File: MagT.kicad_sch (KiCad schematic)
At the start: 6 parts, among them IC6 DRV8212DSGR, IC7 DRV8212DSGR, IC8 DRV8212DSGR

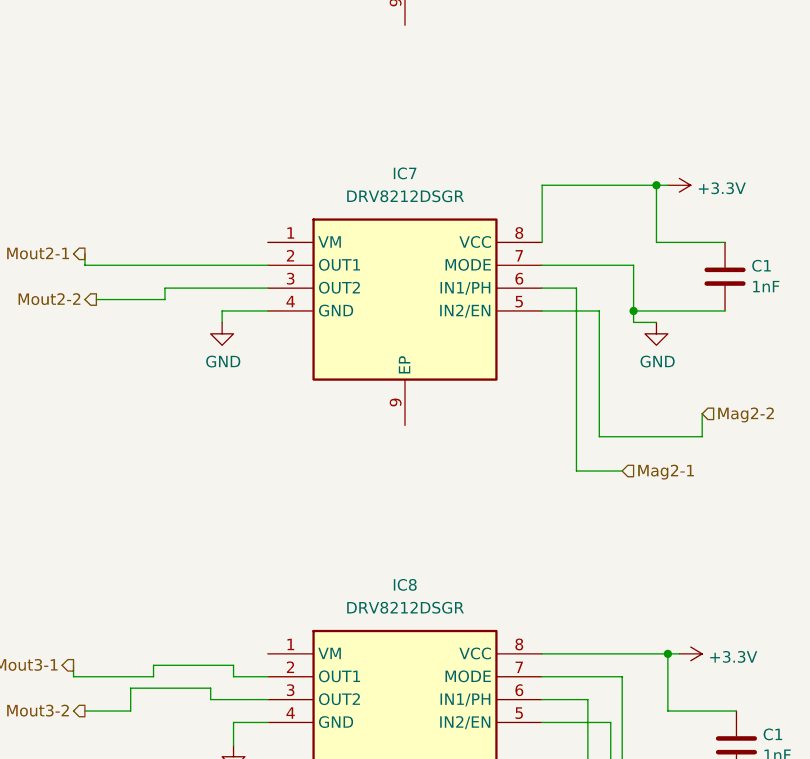
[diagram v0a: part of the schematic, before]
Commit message: Magnetometer fixes\n\nCloses #2
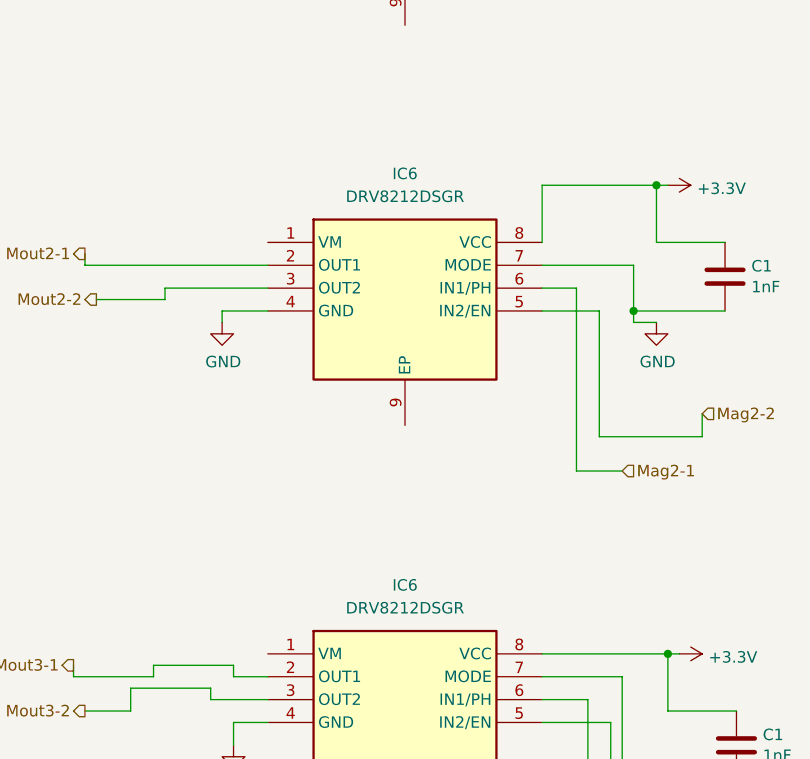
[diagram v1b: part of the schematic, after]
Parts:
- renumbered IC8 to IC6, IC7 to IC6
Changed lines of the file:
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@@
   (symbol (lib_id "power:GND") (at 66.04 63.5 0) (unit 1)
     (in_bom yes) (on_board yes) (dnp no)
-    (property "Reference" "#PWR03" (at 66.04 69.85 0)
+    (property "Reference" "#PWR0106" (at 66.04 69.85 0)
       (effects (font (size 1.27 1.27)) hide)
     )
@@
   (symbol (lib_id "power:GND") (at 63.5 107.95 0) (unit 1)
     (in_bom yes) (on_board yes) (dnp no)
-    (property "Reference" "#PWR04" (at 63.5 114.3 0)
+    (property "Reference" "#PWR0106" (at 63.5 114.3 0)
       (effects (font (size 1.27 1.27)) hide)
     )
@@
   (symbol (lib_id "DRV8212DSGR:DRV8212DSGR") (at 68.58 144.78 0) (unit 1)
     (in_bom yes) (on_board yes) (dnp no) (fields_autoplaced)
-    (property "Reference" "IC8" (at 83.82 137.16 0)
+    (property "Reference" "IC6" (at 83.82 137.16 0)
       (effects (font (size 1.27 1.27)))
     )
@@
   (symbol (lib_id "power:GND") (at 64.77 154.94 0) (unit 1)
     (in_bom yes) (on_board yes) (dnp no)
-    (property "Reference" "#PWR05" (at 64.77 161.29 0)
+    (property "Reference" "#PWR0106" (at 64.77 161.29 0)
       (effects (font (size 1.27 1.27)) hide)
     )
@@
   (symbol (lib_id "DRV8212DSGR:DRV8212DSGR") (at 68.58 99.06 0) (unit 1)
     (in_bom yes) (on_board yes) (dnp no) (fields_autoplaced)
-    (property "Reference" "IC7" (at 83.82 91.44 0)
-      (effects (font (size 1.27 1.27)))
-    )
+    (property "Reference" "IC6" (at 83.82 91.44 0)
+      (effects (font (size 1.27 1.27)))
+    )

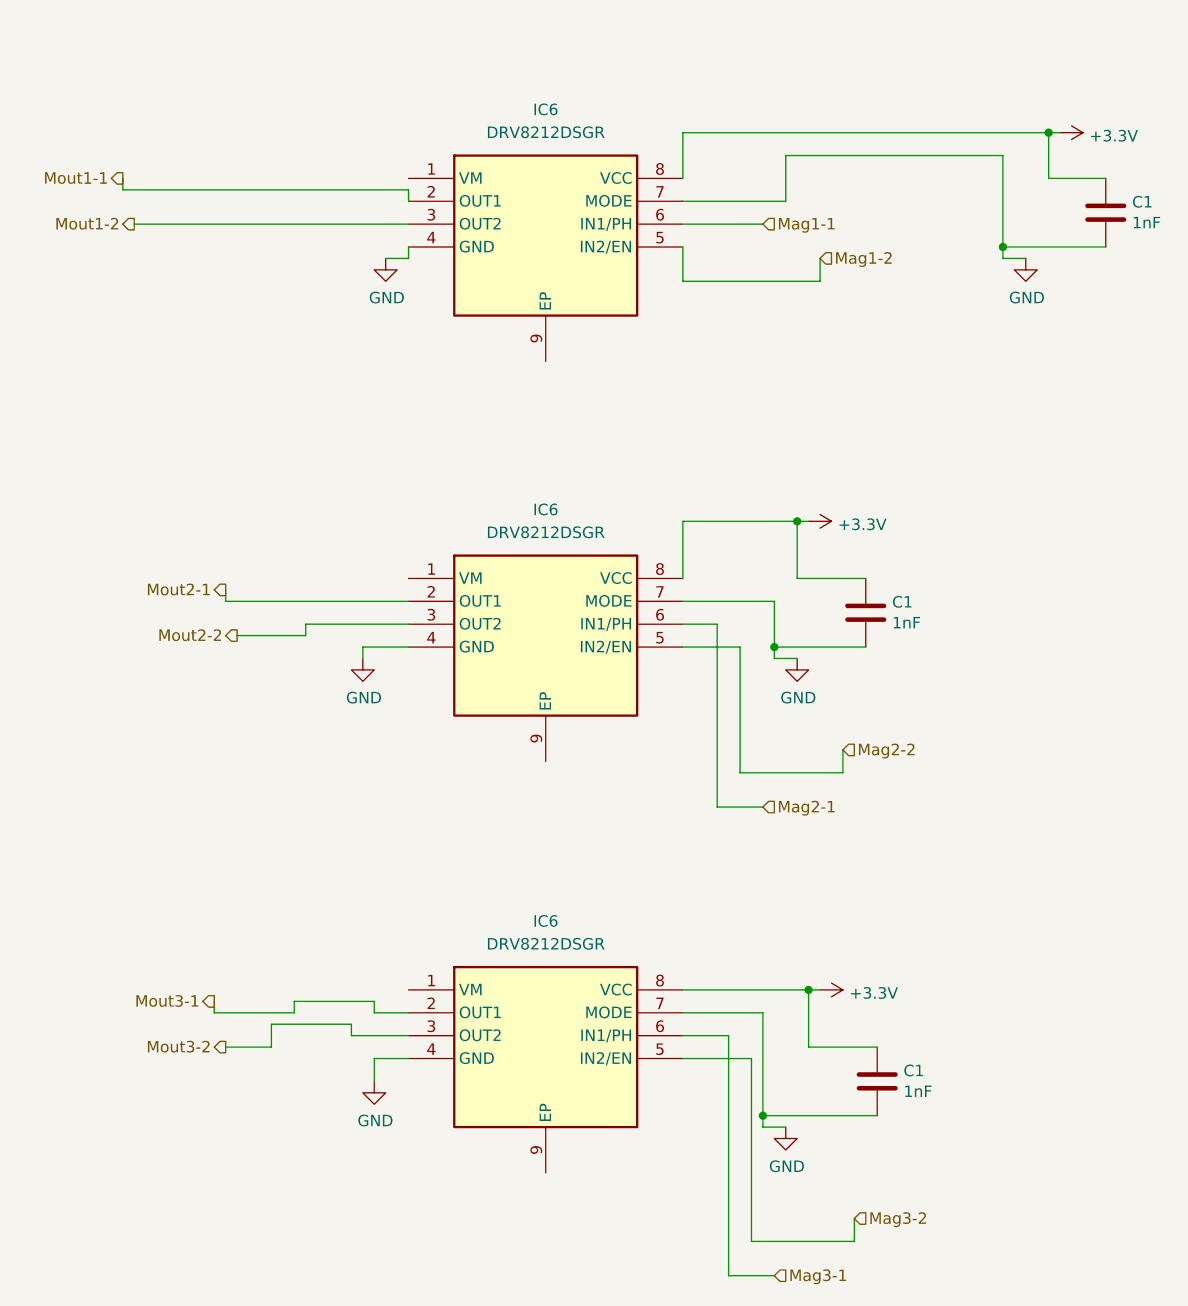
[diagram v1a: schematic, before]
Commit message: Add I2C multiplexer
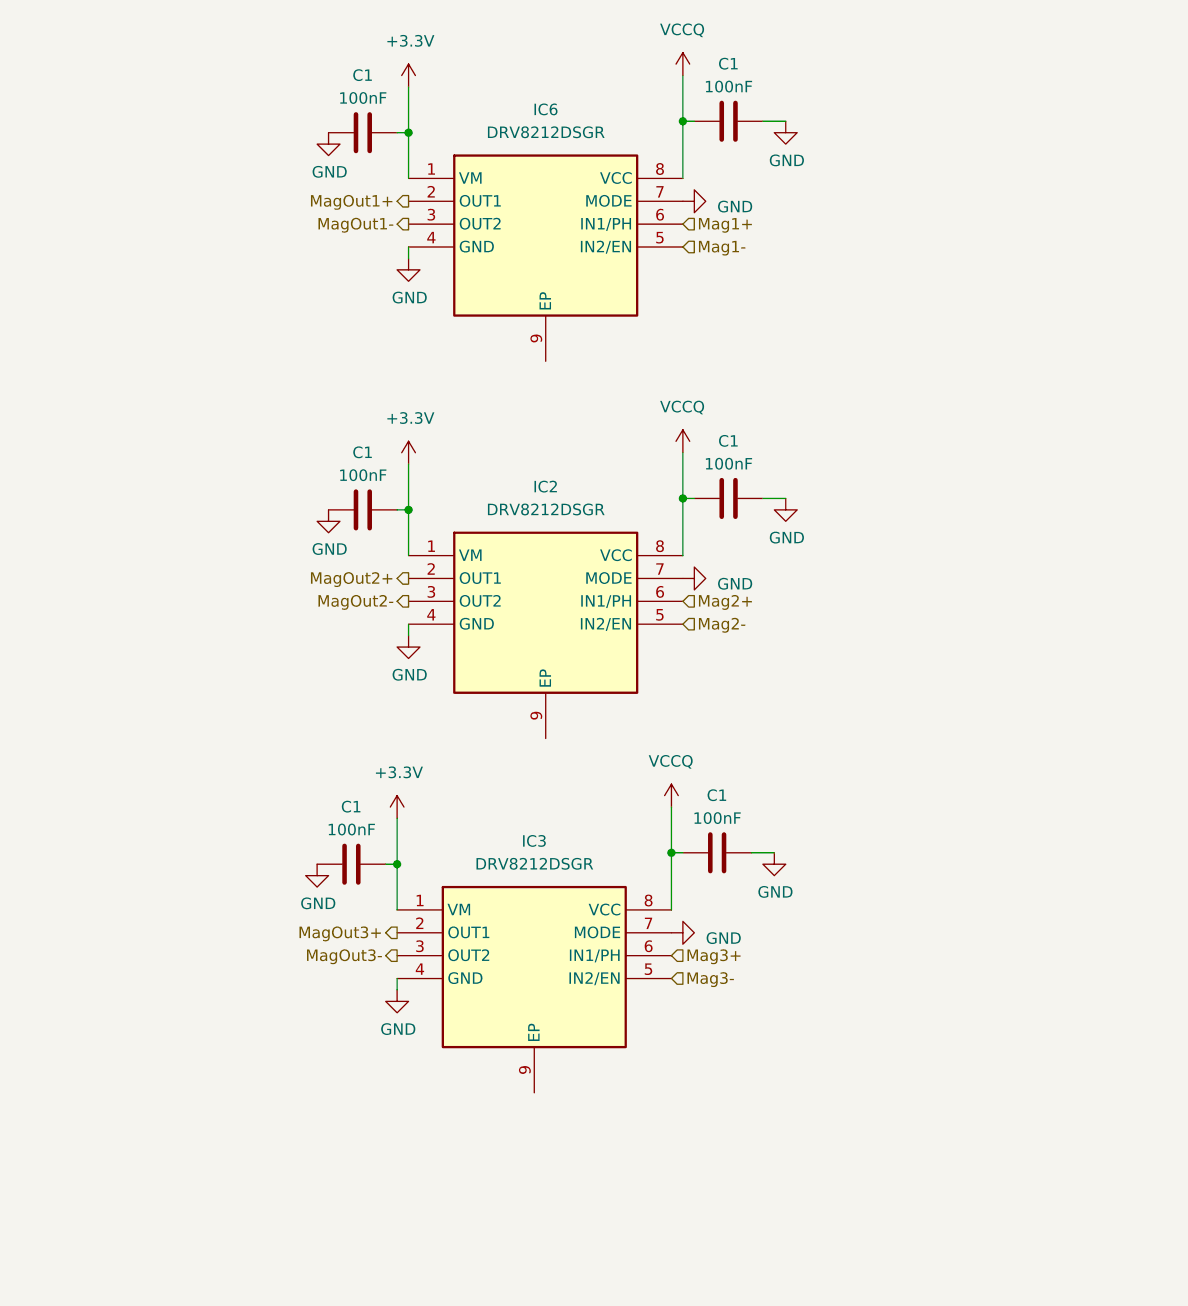
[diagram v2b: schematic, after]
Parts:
- removed C1 (x2): 1nF, Capacitor_SMD:C_0603_1608Metric, symbol Device:C
- removed IC6 (x2): DRV8212DSGR, SON50P200X200X80-9N, symbol DRV8212DSGR:DRV8212DSGR
- added C1 (x5): 100nF, Capacitor_SMD:C_0603_1608Metric, symbol Device:C
- added IC2, IC3: DRV8212DSGR, SON50P200X200X80-9N, symbol DRV8212DSGR:DRV8212DSGR
- C1: value 1nF -> 100nF
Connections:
- net +3V3: now also IC6.1 (VM), C1.1, C1.1, C1.2, C1.2, C1.2, IC2.1 (VM), IC2.8 (VCC), IC3.1 (VM), IC3.8 (VCC)
- net GND: now also C1.1, C1.1, C1.1, C1.2, C1.2, IC2.4 (GND), IC2.7 (MODE), IC3.4 (GND), IC3.7 (MODE)
- net Mag1-1 renamed Mag1+
- net Mag1-2 renamed Mag1-
- net Mout1-1 renamed MagOut1+
- net Mout1-2 renamed MagOut1-
- new net Mag2+: IC2.6 (IN1/PH)
- new net Mag2-: IC2.5 (IN2/EN)
- new net Mag3+: IC3.6 (IN1/PH)
- new net Mag3-: IC3.5 (IN2/EN)
- new net MagOut2+: IC2.2 (OUT1)
- new net MagOut2-: IC2.3 (OUT2)
- new net MagOut3+: IC3.2 (OUT1)
- new net MagOut3-: IC3.3 (OUT2)
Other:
- moved on the sheet: C1

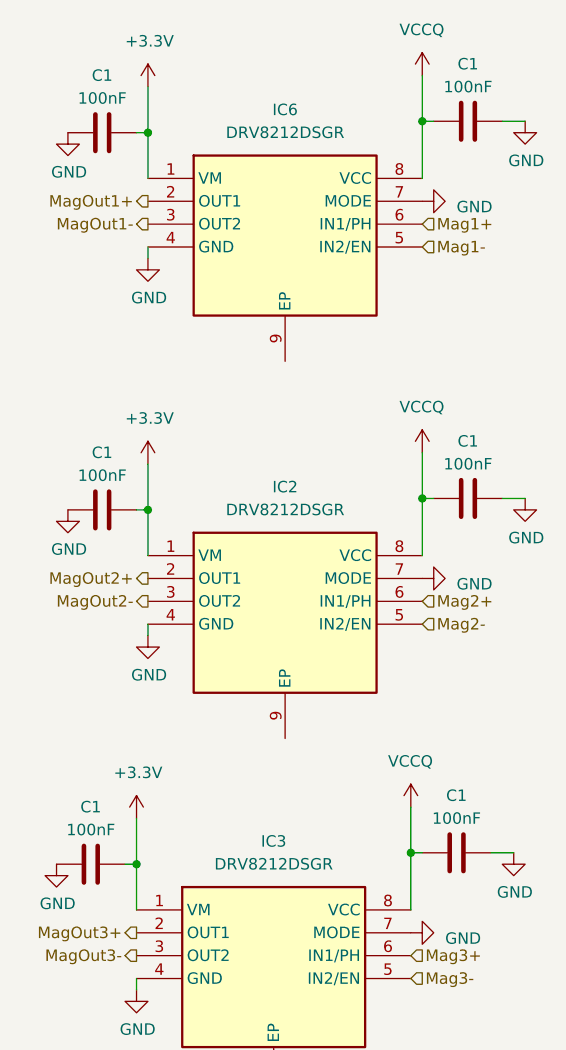
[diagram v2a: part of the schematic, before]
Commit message: Reannotate schematic
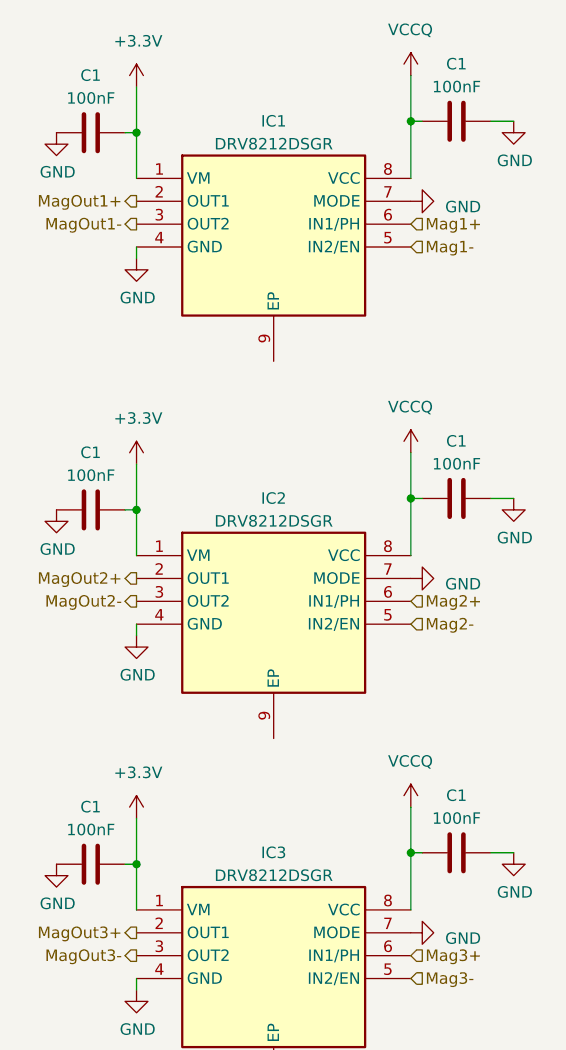
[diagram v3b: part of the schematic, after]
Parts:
- renumbered IC6 to IC1
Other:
- moved on the sheet: C1, IC1, IC2

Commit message: Create PCB layout and routing
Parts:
- IC1, IC2, IC3: footprint SON50P200X200X80-9N -> Library1:SON50P200X200X80-9N
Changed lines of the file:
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@@
       (effects (font (size 1.27 1.27)))
     )
-    (property "Footprint" "SON50P200X200X80-9N" (at 93.98 191.44 0)
+    (property "Footprint" "Library1:SON50P200X200X80-9N" (at 93.98 191.44 0)
       (effects (font (size 1.27 1.27)) (justify left top) hide)
     )
@@
       (effects (font (size 1.27 1.27)))
     )
-    (property "Footprint" "SON50P200X200X80-9N" (at 93.98 230.81 0)
+    (property "Footprint" "Library1:SON50P200X200X80-9N" (at 93.98 230.81 0)
       (effects (font (size 1.27 1.27)) (justify left top) hide)
     )
@@
       (effects (font (size 1.27 1.27)))
     )
-    (property "Footprint" "SON50P200X200X80-9N" (at 93.98 149.53 0)
-      (effects (font (size 1.27 1.27)) (justify left top) hide)
-    )
+    (property "Footprint" "Library1:SON50P200X200X80-9N" (at 93.98 149.53 0)
+      (effects (font (size 1.27 1.27)) (justify left top) hide)
+    )

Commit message: Fix some issues
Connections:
- net +3V3 renamed +3.3VP
- net +3.3VP: no longer C1.1, C1.1, C1.1, IC1.8 (VCC), IC2.8 (VCC), IC3.8 (VCC)
- new net VCCQ: C1.1, C1.1, C1.1, IC1.8 (VCC), IC2.8 (VCC), IC3.8 (VCC)
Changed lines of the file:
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@@
     (effects (font (size 1.27 1.27)) (justify left))
-  )
-  (symbol (lib_id "power:+3.3V") (at 67.31 86.36 0) (unit 1)
-    (in_bom yes) (on_board yes) (dnp no)
-    (property "Reference" "#PWR023" (at 67.31 90.17 0)
-      (effects (font (size 1.27 1.27)) hide)
-    )
-    (property "Value" "+3.3V" (at 64.77 81.28 0)
-      (effects (font (size 1.27 1.27)) (justify left))
-    )
-    (property "Footprint" "" (at 67.31 86.36 0)
-      (effects (font (size 1.27 1.27)) hide)
-    )
-    (property "Datasheet" "" (at 67.31 86.36 0)
-      (effects (font (size 1.27 1.27)) hide)
-    )
-    (pin "1")
-    (instances
-      (project "NEW_PCB_ADCS"
-        (path "/42c40d7d-71af-4ce9-bac9-d638f259c957"
-          (reference "#PWR023") (unit 1)
-        )
-        (path "/42c40d7d-71af-4ce9-bac9-d638f259c957/2b7bfac4-b78d-4444-8160-12b42cf2429b"
-          (reference "#PWR042") (unit 1)
-        )
-      )
-      (project "pq9ish-main-hw"
-        (path "/619b49ed-1bcd-4c84-8c0f-98372f01728f"
-          (reference "#PWR023") (unit 1)
-        )
-      )
-    )
   )
   (symbol (lib_id "Device:C") (at 102.87 129.54 90) (unit 1)
@@
     )
   )
+  (symbol (lib_id "power:+3.3VP") (at 67.31 86.36 0) (unit 1)
+    (in_bom yes) (on_board yes) (dnp no) (fields_autoplaced)
+    (property "Reference" "#PWR060" (at 71.12 87.63 0)
+      (effects (font (size 1.27 1.27)) hide)
+    )
+    (property "Value" "+3.3VP" (at 67.31 82.55 0)
+      (effects (font (size 1.27 1.27)))
+    )
+    (property "Footprint" "" (at 67.31 86.36 0)
+      (effects (font (size 1.27 1.27)) hide)
+    )
+    (property "Datasheet" "" (at 67.31 86.36 0)
+      (effects (font (size 1.27 1.27)) hide)
+    )
+    (pin "1")
+    (instances
+      (project "NEW_PCB_ADCS"
+        (path "/42c40d7d-71af-4ce9-bac9-d638f259c957/00000000-0000-0000-0000-00005a289551"
+          (reference "#PWR060") (unit 1)
+        )
+        (path "/42c40d7d-71af-4ce9-bac9-d638f259c957/2b7bfac4-b78d-4444-8160-12b42cf2429b"
+          (reference "#PWR042") (unit 1)
+        )
+      )
+    )
+  )
   (symbol (lib_id "power:GND") (at 97.79 138.43 90) (unit 1)
     (in_bom yes) (on_board yes) (dnp no) (fields_autoplaced)
@@
     )
   )
-  (symbol (lib_id "power:+3.3V") (at 67.31 125.73 0) (unit 1)
-    (in_bom yes) (on_board yes) (dnp no)
-    (property "Reference" "#PWR023" (at 67.31 129.54 0)
-      (effects (font (size 1.27 1.27)) hide)
-    )
-    (property "Value" "+3.3V" (at 64.77 120.65 0)
-      (effects (font (size 1.27 1.27)) (justify left))
-    )
-    (property "Footprint" "" (at 67.31 125.73 0)
-      (effects (font (size 1.27 1.27)) hide)
-    )
-    (property "Datasheet" "" (at 67.31 125.73 0)
-      (effects (font (size 1.27 1.27)) hide)
-    )
-    (pin "1")
-    (instances
-      (project "NEW_PCB_ADCS"
-        (path "/42c40d7d-71af-4ce9-bac9-d638f259c957"
-          (reference "#PWR023") (unit 1)
-        )
-        (path "/42c40d7d-71af-4ce9-bac9-d638f259c957/2b7bfac4-b78d-4444-8160-12b42cf2429b"
-          (reference "#PWR044") (unit 1)
-        )
-      )
-      (project "pq9ish-main-hw"
-        (path "/619b49ed-1bcd-4c84-8c0f-98372f01728f"
-          (reference "#PWR023") (unit 1)
-        )
-      )
-    )
-  )
-  (symbol (lib_id "power:+3.3V") (at 97.79 124.46 0) (unit 1)
+  (symbol (lib_id "power:VCCQ") (at 97.79 124.46 0) (unit 1)
     (in_bom yes) (on_board yes) (dnp no)
     (property "Reference" "#PWR023" (at 97.79 128.27 0)
@@
     )
   )
+  (symbol (lib_id "power:+3.3VP") (at 67.31 44.45 0) (unit 1)
+    (in_bom yes) (on_board yes) (dnp no) (fields_autoplaced)
+    (property "Reference" "#PWR060" (at 71.12 45.72 0)
+      (effects (font (size 1.27 1.27)) hide)
+    )
+    (property "Value" "+3.3VP" (at 67.31 40.64 0)
+      (effects (font (size 1.27 1.27)))
+    )
+    (property "Footprint" "" (at 67.31 44.45 0)
+      (effects (font (size 1.27 1.27)) hide)
+    )
+    (property "Datasheet" "" (at 67.31 44.45 0)
+      (effects (font (size 1.27 1.27)) hide)
+    )
+    (pin "1")
+    (instances
+      (project "NEW_PCB_ADCS"
+        (path "/42c40d7d-71af-4ce9-bac9-d638f259c957/00000000-0000-0000-0000-00005a289551"
+          (reference "#PWR060") (unit 1)
+        )
+        (path "/42c40d7d-71af-4ce9-bac9-d638f259c957/2b7bfac4-b78d-4444-8160-12b42cf2429b"
+          (reference "#PWR040") (unit 1)
+        )
+      )
+    )
+  )
   (symbol (lib_id "Device:C") (at 62.23 49.53 90) (unit 1)
     (in_bom yes) (on_board yes) (dnp no) (fields_autoplaced)
@@
     )
   )
-  (symbol (lib_id "power:+3.3V") (at 67.31 44.45 0) (unit 1)
-    (in_bom yes) (on_board yes) (dnp no)
-    (property "Reference" "#PWR023" (at 67.31 48.26 0)
-      (effects (font (size 1.27 1.27)) hide)
-    )
-    (property "Value" "+3.3V" (at 64.77 39.37 0)
-      (effects (font (size 1.27 1.27)) (justify left))
-    )
-    (property "Footprint" "" (at 67.31 44.45 0)
-      (effects (font (size 1.27 1.27)) hide)
-    )
-    (property "Datasheet" "" (at 67.31 44.45 0)
-      (effects (font (size 1.27 1.27)) hide)
-    )
-    (pin "1")
-    (instances
-      (project "NEW_PCB_ADCS"
-        (path "/42c40d7d-71af-4ce9-bac9-d638f259c957"
-          (reference "#PWR023") (unit 1)
-        )
-        (path "/42c40d7d-71af-4ce9-bac9-d638f259c957/2b7bfac4-b78d-4444-8160-12b42cf2429b"
-          (reference "#PWR040") (unit 1)
-        )
-      )
-      (project "pq9ish-main-hw"
-        (path "/619b49ed-1bcd-4c84-8c0f-98372f01728f"
-          (reference "#PWR023") (unit 1)
-        )
-      )
-    )
-  )
-  (symbol (lib_id "power:+3.3V") (at 97.79 43.18 0) (unit 1)
+  (symbol (lib_id "power:VCCQ") (at 97.79 43.18 0) (unit 1)
     (in_bom yes) (on_board yes) (dnp no)
     (property "Reference" "#PWR023" (at 97.79 46.99 0)
@@
     )
   )
-  (symbol (lib_id "power:+3.3V") (at 97.79 85.09 0) (unit 1)
+  (symbol (lib_id "power:+3.3VP") (at 67.31 125.73 0) (unit 1)
+    (in_bom yes) (on_board yes) (dnp no) (fields_autoplaced)
+    (property "Reference" "#PWR060" (at 71.12 127 0)
+      (effects (font (size 1.27 1.27)) hide)
+    )
+    (property "Value" "+3.3VP" (at 67.31 121.92 0)
+      (effects (font (size 1.27 1.27)))
+    )
+    (property "Footprint" "" (at 67.31 125.73 0)
+      (effects (font (size 1.27 1.27)) hide)
+    )
+    (property "Datasheet" "" (at 67.31 125.73 0)
+      (effects (font (size 1.27 1.27)) hide)
+    )
+    (pin "1")
+    (instances
+      (project "NEW_PCB_ADCS"
+        (path "/42c40d7d-71af-4ce9-bac9-d638f259c957/00000000-0000-0000-0000-00005a289551"
+          (reference "#PWR060") (unit 1)
+        )
+        (path "/42c40d7d-71af-4ce9-bac9-d638f259c957/2b7bfac4-b78d-4444-8160-12b42cf2429b"
+          (reference "#PWR044") (unit 1)
+        )
+      )
+    )
+  )
+  (symbol (lib_id "power:VCCQ") (at 97.79 85.09 0) (unit 1)
     (in_bom yes) (on_board yes) (dnp no)
     (property "Reference" "#PWR023" (at 97.79 88.9 0)

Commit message: Use pogo pins; move diode to back
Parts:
- IC1, IC2, IC3: MPN (none) -> DRV8212DSGR
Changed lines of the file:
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@@
       (effects (font (size 1.27 1.27)) (justify left top) hide)
+    )
+    (property "MPN" "DRV8212DSGR" (at 67.31 96.52 0)
+      (effects (font (size 1.27 1.27)) hide)
     )
     (pin "1")
@@
       (effects (font (size 1.27 1.27)) (justify left top) hide)
     )
+    (property "MPN" "DRV8212DSGR" (at 67.31 135.89 0)
+      (effects (font (size 1.27 1.27)) hide)
+    )
     (pin "1")
     (pin "2")
@@
       (effects (font (size 1.27 1.27)) (justify left top) hide)
     )
-    (pin "1")
+    (property "MPN" "DRV8212DSGR" (at 67.31 54.61 0)
+      (effects (font (size 1.27 1.27)) hide)
+    )
+    (pin "1")
